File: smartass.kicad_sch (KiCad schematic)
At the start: 0 parts

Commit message: Completed content of Connectors sheet, started SmartAss sheet
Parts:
- added PL9-A?: DB15_Female, symbol Connector:DB15_Female
- added PL9-B?: DB15_Male, symbol Connector:DB15_Male
- added RV?: Volume, symbol Device:R_Potentiometer
- added SW?: On/Off, symbol Switch:SW_SPST
- added SW?: Select, symbol Switch:SW_Push
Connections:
- new net: PL9-A?.1, SW?.1 (A)
- new net: PL9-A?.2, SW?.2 (B)
- new net: PL9-A?.3, RV?.2
- new net: PL9-A?.4, RV?.3
- new net: PL9-A?.5, SW?.1
- new net: PL9-A?.6, SW?.2
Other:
- note added: "SmartAss Speaking ASI Control Panel"
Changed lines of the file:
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@@
 (kicad_sch (version 20211123) (generator eeschema)
   (paper "A4")
+  (polyline (pts (xy 81.915 61.595) (xy 81.915 114.935))
+    (stroke (width 0) (type default) (color 0 0 0 0))
+  )
+  (polyline (pts (xy 43.815 64.135) (xy 43.815 104.775))
+    (stroke (width 0) (type default) (color 0 0 0 0))
+  )
+  (wire (pts (xy 28.575 94.615) (xy 85.725 94.615))
+    (stroke (width 0) (type default) (color 0 0 0 0))
+  )
+  (polyline (pts (xy 43.815 104.775) (xy 24.765 104.775))
+    (stroke (width 0) (type default) (color 0 0 0 0))
+  )
+  (wire (pts (xy 29.845 74.295) (xy 85.725 74.295))
+    (stroke (width 0) (type default) (color 0 0 0 0))
+  )
+  (polyline (pts (xy 111.125 114.935) (xy 81.915 114.935))
+    (stroke (width 0) (type default) (color 0 0 0 0))
+  )
+  (wire (pts (xy 28.575 94.615) (xy 28.575 99.695))
+    (stroke (width 0) (type default) (color 0 0 0 0))
+  )
+  (polyline (pts (xy 24.765 104.775) (xy 24.765 64.135))
+    (stroke (width 0) (type default) (color 0 0 0 0))
+  )
+  (wire (pts (xy 37.465 89.535) (xy 85.725 89.535))
+    (stroke (width 0) (type default) (color 0 0 0 0))
+  )
+  (polyline (pts (xy 81.915 61.595) (xy 111.125 61.595))
+    (stroke (width 0) (type default) (color 0 0 0 0))
+  )
+  (wire (pts (xy 40.005 79.375) (xy 85.725 79.375))
+    (stroke (width 0) (type default) (color 0 0 0 0))
+  )
+  (wire (pts (xy 38.735 99.695) (xy 85.725 99.695))
+    (stroke (width 0) (type default) (color 0 0 0 0))
+  )
+  (polyline (pts (xy 111.125 61.595) (xy 111.125 114.935))
+    (stroke (width 0) (type default) (color 0 0 0 0))
+  )
+  (wire (pts (xy 33.655 84.455) (xy 85.725 84.455))
+    (stroke (width 0) (type default) (color 0 0 0 0))
+  )
+  (wire (pts (xy 33.655 85.725) (xy 33.655 84.455))
+    (stroke (width 0) (type default) (color 0 0 0 0))
+  )
+  (polyline (pts (xy 24.765 64.135) (xy 43.815 64.135))
+    (stroke (width 0) (type default) (color 0 0 0 0))
+  )
+  (wire (pts (xy 29.845 79.375) (xy 29.845 74.295))
+    (stroke (width 0) (type default) (color 0 0 0 0))
+  )
+  (text "SmartAss\nSpeaking ASI\nControl Panel" (at 26.035 71.755 0)
+    (effects (font (size 1.27 1.27)) (justify left bottom))
+  )
+  (symbol (lib_id "Switch:SW_SPST") (at 34.925 79.375 0) (unit 1)
+    (in_bom yes) (on_board yes)
+    (property "Reference" "SW?" (id 0) (at 36.1951 80.645 90)
+      (effects (font (size 1.27 1.27)) (justify right) hide)
+    )
+    (property "Value" "On/Off" (id 1) (at 37.465 81.915 0)
+      (effects (font (size 1.27 1.27)) (justify right))
+    )
+    (property "Footprint" "" (id 2) (at 34.925 79.375 0)
+      (effects (font (size 1.27 1.27)) hide)
+    )
+    (property "Datasheet" "~" (id 3) (at 34.925 79.375 0)
+      (effects (font (size 1.27 1.27)) hide)
+    )
+    (pin "1")
+    (pin "2")
+  )
+  (symbol (lib_id "Device:R_Potentiometer") (at 33.655 89.535 90) (unit 1)
+    (in_bom yes) (on_board yes)
+    (property "Reference" "RV?" (id 0) (at 33.655 93.345 90)
+      (effects (font (size 1.27 1.27)) hide)
+    )
+    (property "Value" "Volume" (id 1) (at 33.655 92.075 90))
+    (property "Footprint" "" (id 2) (at 33.655 89.535 0)
+      (effects (font (size 1.27 1.27)) hide)
+    )
+    (property "Datasheet" "~" (id 3) (at 33.655 89.535 0)
+      (effects (font (size 1.27 1.27)) hide)
+    )
+    (pin "1")
+    (pin "2")
+    (pin "3")
+  )
+  (symbol (lib_id "Connector:DB15_Female") (at 93.345 92.075 0) (unit 1)
+    (in_bom yes) (on_board yes)
+    (property "Reference" "PL9-A?" (id 0) (at 88.265 65.405 0)
+      (effects (font (size 1.27 1.27)) (justify left))
+    )
+    (property "Value" "DB15_Female" (id 1) (at 81.915 67.945 0)
+      (effects (font (size 1.27 1.27)) (justify left))
+    )
+    (property "Footprint" "" (id 2) (at 93.345 92.075 0)
+      (effects (font (size 1.27 1.27)) hide)
+    )
+    (property "Datasheet" " ~" (id 3) (at 93.345 92.075 0)
+      (effects (font (size 1.27 1.27)) hide)
+    )
+    (pin "1")
+    (pin "10")
+    (pin "11")
+    (pin "12")
+    (pin "13")
+    (pin "14")
+    (pin "15")
+    (pin "2")
+    (pin "3")
+    (pin "4")
+    (pin "5")
+    (pin "6")
+    (pin "7")
+    (pin "8")
+    (pin "9")
+  )
+  (symbol (lib_id "Switch:SW_Push") (at 33.655 99.695 0) (unit 1)
+    (in_bom yes) (on_board yes)
+    (property "Reference" "SW?" (id 0) (at 33.655 92.075 0)
+      (effects (font (size 1.27 1.27)) hide)
+    )
+    (property "Value" "Select" (id 1) (at 33.655 100.965 0))
+    (property "Footprint" "" (id 2) (at 33.655 94.615 0)
+      (effects (font (size 1.27 1.27)) hide)
+    )
+    (property "Datasheet" "~" (id 3) (at 33.655 94.615 0)
+      (effects (font (size 1.27 1.27)) hide)
+    )
+    (pin "1")
+    (pin "2")
+  )
+  (symbol (lib_id "Connector:DB15_Male") (at 100.965 92.075 180) (unit 1)
+    (in_bom yes) (on_board yes) (fields_autoplaced)
+    (property "Reference" "PL9-B?" (id 0) (at 101.2825 65.405 0))
+    (property "Value" "DB15_Male" (id 1) (at 101.2825 67.945 0))
+    (property "Footprint" "" (id 2) (at 100.965 92.075 0)
+      (effects (font (size 1.27 1.27)) hide)
+    )
+    (property "Datasheet" " ~" (id 3) (at 100.965 92.075 0)
+      (effects (font (size 1.27 1.27)) hide)
+    )
+    (pin "1")
+    (pin "10")
+    (pin "11")
+    (pin "12")
+    (pin "13")
+    (pin "14")
+    (pin "15")
+    (pin "2")
+    (pin "3")
+    (pin "4")
+    (pin "5")
+    (pin "6")
+    (pin "7")
+    (pin "8")
+    (pin "9")
+  )
 )

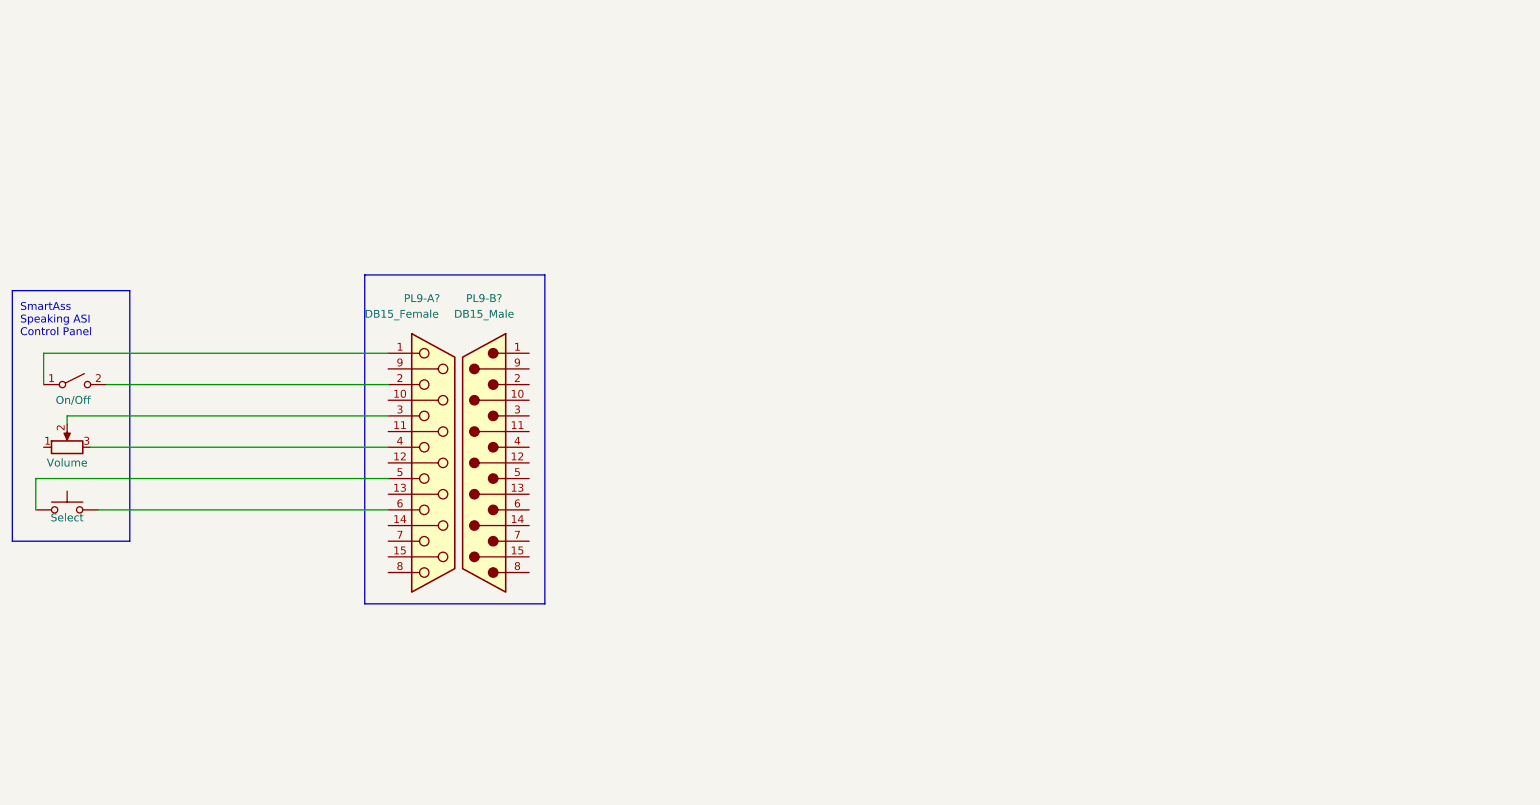
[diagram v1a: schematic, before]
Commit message: Small updates to multiple sheets, and major update to SmartAss sheet
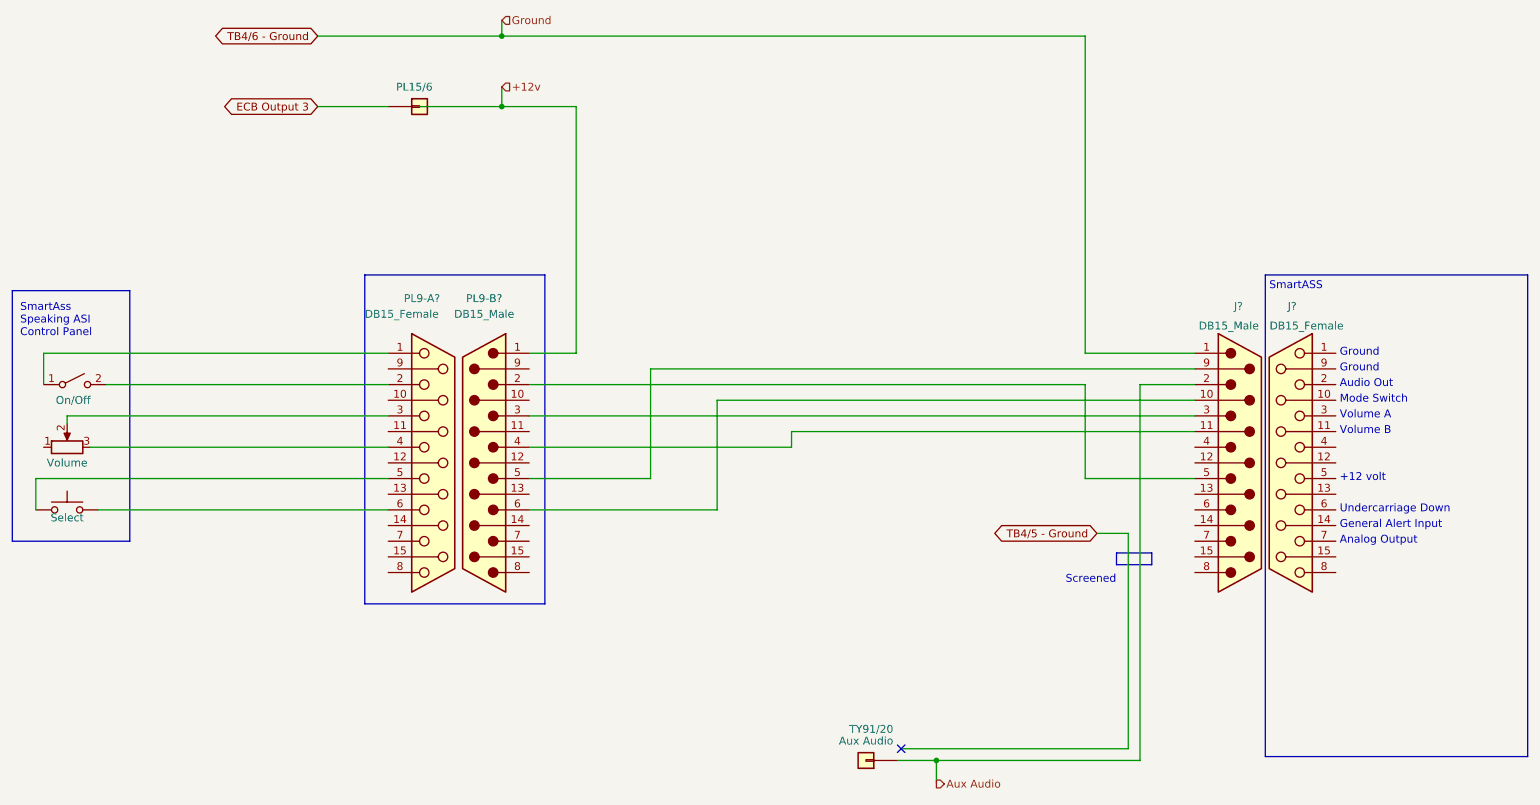
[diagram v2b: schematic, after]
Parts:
- added J?: DB15_Female, symbol Connector:DB15_Female
- added J?: DB15_Male, symbol Connector:DB15_Male
- added PL15/6: Conn_01x01, symbol Connector_Generic:Conn_01x01
- added TY91/20: Aux Audio, symbol Connector_Generic:Conn_01x01
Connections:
- net +12v: now reaches PL9-B?.1
- net at PL9-B?.2: now also J?.5
- net at PL9-B?.3: now also J?.3
- net at PL9-B?.4: now also J?.11 (P111)
- net at PL9-B?.5: now also J?.9 (P9)
- net at PL9-B?.6: now also J?.10 (P10)
- new net Aux Audio: J?.2, TY91/20.1 (Pin_1)
- new net ECB Output 3: PL15/6.1 (Pin_1)
- new net TB4/6 - Ground: J?.1
- no-connect marks 0 -> 1
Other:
- note added: "+12 volt"
- note added: "Analog Output"
- note added: "Audio Out"
- note added: "General Alert Input"
- note added: "Ground"
- note added: "Mode Switch"
- note added: "Screened"
- note added: "SmartASS"
- note added: "Undercarriage Down"
- note added: "Volume A"
- note added: "Volume B"
- title: (none) -> Europa - SmartASS Wiring
